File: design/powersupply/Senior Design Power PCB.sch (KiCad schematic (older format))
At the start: 10 parts, among them U1 INA226, U2 LM2596SX-5

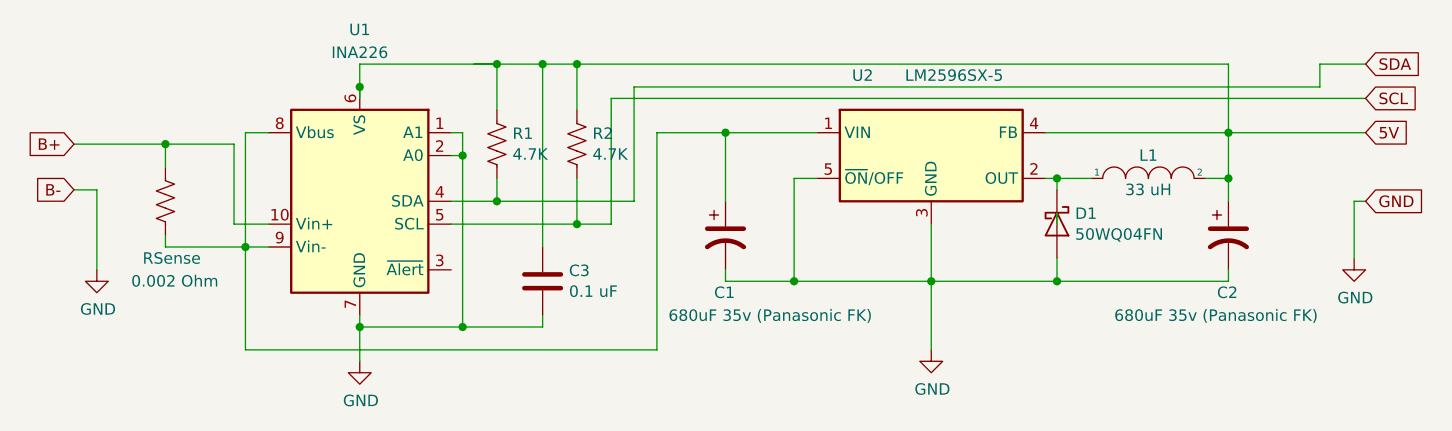
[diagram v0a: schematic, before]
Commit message: fixed power supply schematic
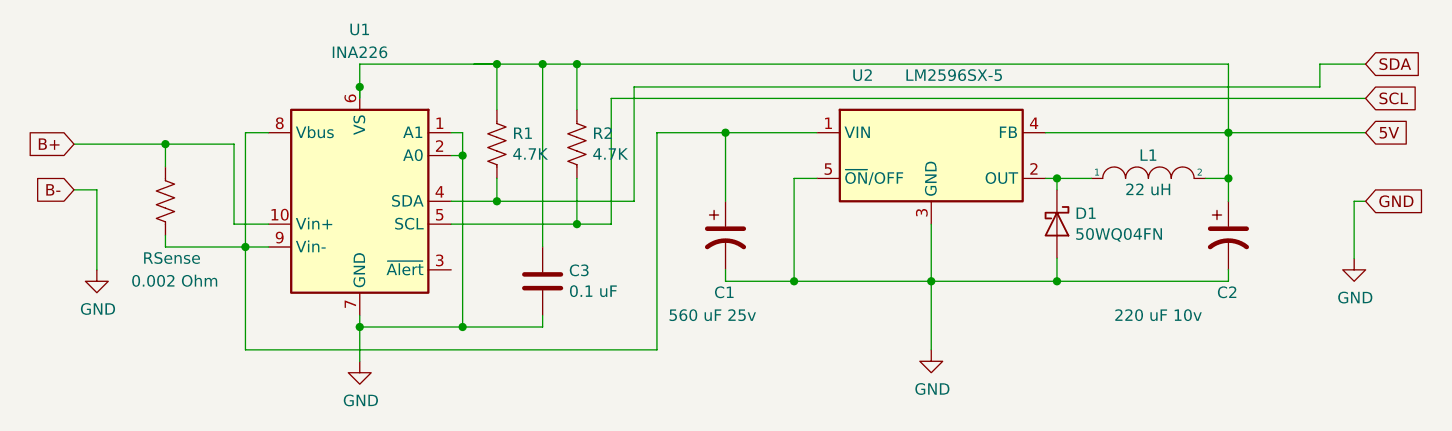
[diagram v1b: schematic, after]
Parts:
- C1: value 680uF 35v (Panasonic FK) -> 560 uF 25v
- C2: value 680uF 35v (Panasonic FK) -> 220 uF 10v
- L1: value 33 uH -> 22 uH
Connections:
- wire segments 72 -> 71
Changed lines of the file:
@@
 EESchema Schematic File Version 4
-LIBS:Senior Design Power PCB-cache
 EELAYER 30 0
 EELAYER END
@@
 P 7200 3600
 F 0 "L1" H 7200 3700 50  0000 C CNN
-F 1 "33 uH" H 7200 3550 50  0000 C CNN
+F 1 "22 uH" H 7200 3550 50  0000 C CNN
 F 2 "" H 7200 3600 50  0001 C CNN
 F 3 "~" H 7200 3600 50  0001 C CNN
@@
 	6800 3600 6800 3650
 Wire Wire Line
-	6800 3750 6800 3800
-Wire Wire Line
 	6250 3800 6250 4050
 $Comp
@@
 P 7550 3850
 F 0 "C2" H 7500 3600 50  0000 L CNN
-F 1 "680uF 35v (Panasonic FK)" H 7050 3500 50  0000 L CNN
+F 1 "220 uF 10v" H 7050 3500 50  0000 L CNN
 F 2 "" H 7550 3850 50  0001 C CNN
 F 3 "~" H 7550 3850 50  0001 C CNN
@@
 P 5350 3850
 F 0 "C1" H 5300 3600 50  0000 L CNN
-F 1 "680uF 35v (Panasonic FK)" H 5100 3500 50  0000 L CNN
+F 1 "560 uF 25v" H 5100 3500 50  0000 L CNN
 F 2 "" H 5350 3850 50  0001 C CNN
 F 3 "~" H 5350 3850 50  0001 C CNN
